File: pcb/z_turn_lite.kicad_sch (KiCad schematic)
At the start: 1 part

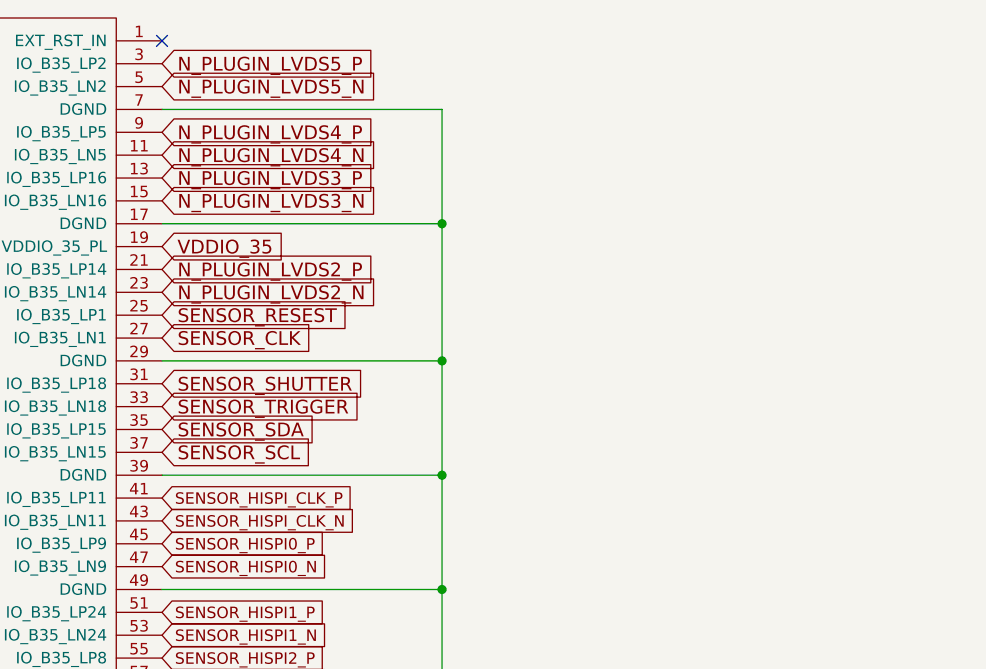
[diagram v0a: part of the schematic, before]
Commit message: refinements; add ar1335 footprint
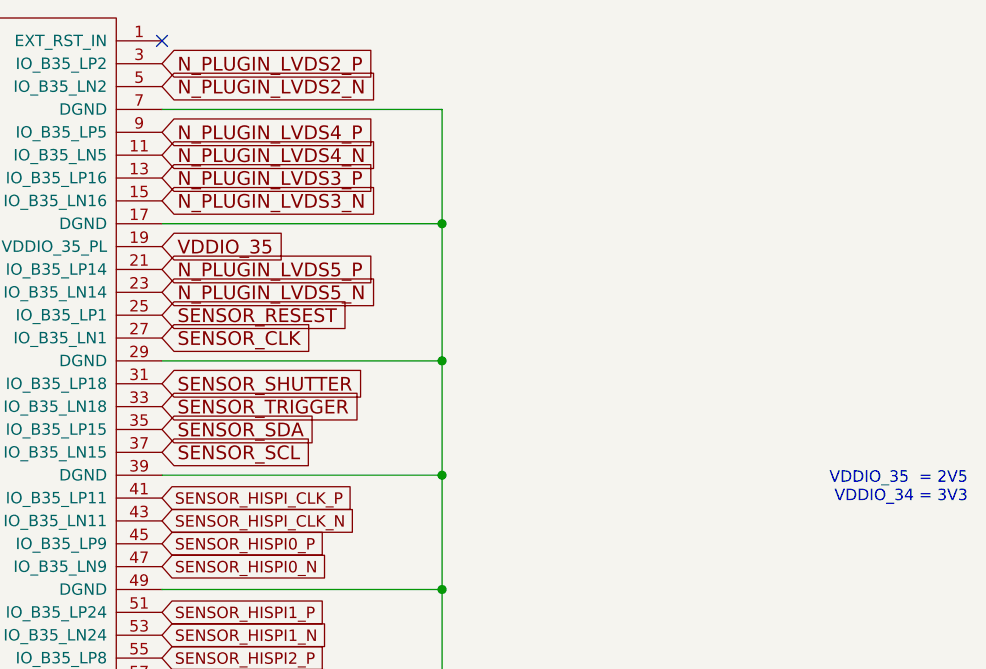
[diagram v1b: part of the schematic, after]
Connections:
- net N_PLUGIN_LVDS2_N: now also A.5 (IO_B35_LN2); no longer A.23 (IO_B35_LN14)
- net N_PLUGIN_LVDS2_P: now also A.3 (IO_B35_LP2); no longer A.21 (IO_B35_LP14)
- net N_PLUGIN_LVDS5_N: now also A.23 (IO_B35_LN14); no longer A.5 (IO_B35_LN2)
- net N_PLUGIN_LVDS5_P: now also A.21 (IO_B35_LP14); no longer A.3 (IO_B35_LP2)
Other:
- note added: "VDDIO_35 = 2V5 VDDIO_34 = 3V3"
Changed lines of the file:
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@@
     (stroke (width 0) (type solid) (color 0 0 0 0))
+  )
+  (text "VDDIO_35  = 2V5\nVDDIO_34 = 3V3" (at 210.82 76.2 180)
+    (effects (font (size 1.27 1.27)) (justify right bottom))
   )
   (global_label "N_PLUGIN_LVDS1_P" (shape input) (at 71.755 27.305 180)    (property "Intersheet References" "${INTERSHEET_REFS}" (id 0) (at 45.4043 27.4002 0)
@@
     (effects (font (size 1.524 1.524)) (justify right))
   )
-  (global_label "N_PLUGIN_LVDS5_P" (shape input) (at 121.285 27.305 0)    (property "Intersheet References" "${INTERSHEET_REFS}" (id 0) (at 147.6357 27.4002 0)
-      (effects (font (size 1.524 1.524)) (justify left) hide)
-    )
-    (effects (font (size 1.524 1.524)) (justify left))
-  )
-  (global_label "N_PLUGIN_LVDS5_N" (shape input) (at 121.285 29.845 0)    (property "Intersheet References" "${INTERSHEET_REFS}" (id 0) (at 147.7083 29.9402 0)
+  (global_label "N_PLUGIN_LVDS2_P" (shape input) (at 121.285 27.305 0)    (property "Intersheet References" "${INTERSHEET_REFS}" (id 0) (at 147.6357 27.2098 0)
+      (effects (font (size 1.524 1.524)) (justify left) hide)
+    )
+    (effects (font (size 1.524 1.524)) (justify left))
+  )
+  (global_label "N_PLUGIN_LVDS2_N" (shape input) (at 121.285 29.845 0)    (property "Intersheet References" "${INTERSHEET_REFS}" (id 0) (at 147.7083 29.7498 0)
       (effects (font (size 1.524 1.524)) (justify left) hide)
     )
@@
     (effects (font (size 1.524 1.524)) (justify left))
   )
-  (global_label "N_PLUGIN_LVDS2_P" (shape input) (at 121.285 50.165 0)    (property "Intersheet References" "${INTERSHEET_REFS}" (id 0) (at 147.6357 50.0698 0)
-      (effects (font (size 1.524 1.524)) (justify left) hide)
-    )
-    (effects (font (size 1.524 1.524)) (justify left))
-  )
-  (global_label "N_PLUGIN_LVDS2_N" (shape input) (at 121.285 52.705 0)    (property "Intersheet References" "${INTERSHEET_REFS}" (id 0) (at 147.7083 52.6098 0)
-      (effects (font (size 1.524 1.524)) (justify left) hide)
-    )
+  (global_label "N_PLUGIN_LVDS5_P" (shape input) (at 121.285 50.165 0)    (property "Intersheet References" "${INTERSHEET_REFS}" (id 0) (at 147.6357 50.2602 0)
+      (effects (font (size 1.524 1.524)) (justify left) hide)
+    )
+    (effects (font (size 1.524 1.524)) (justify left))
+  )
+  (global_label "N_PLUGIN_LVDS5_N" (shape input) (at 121.285 52.705 0)    (property "Intersheet References" "${INTERSHEET_REFS}" (id 0) (at 147.7083 52.8002 0)
+      (effects (font (size 1.524 1.524)) (justify left) hide)
+    )

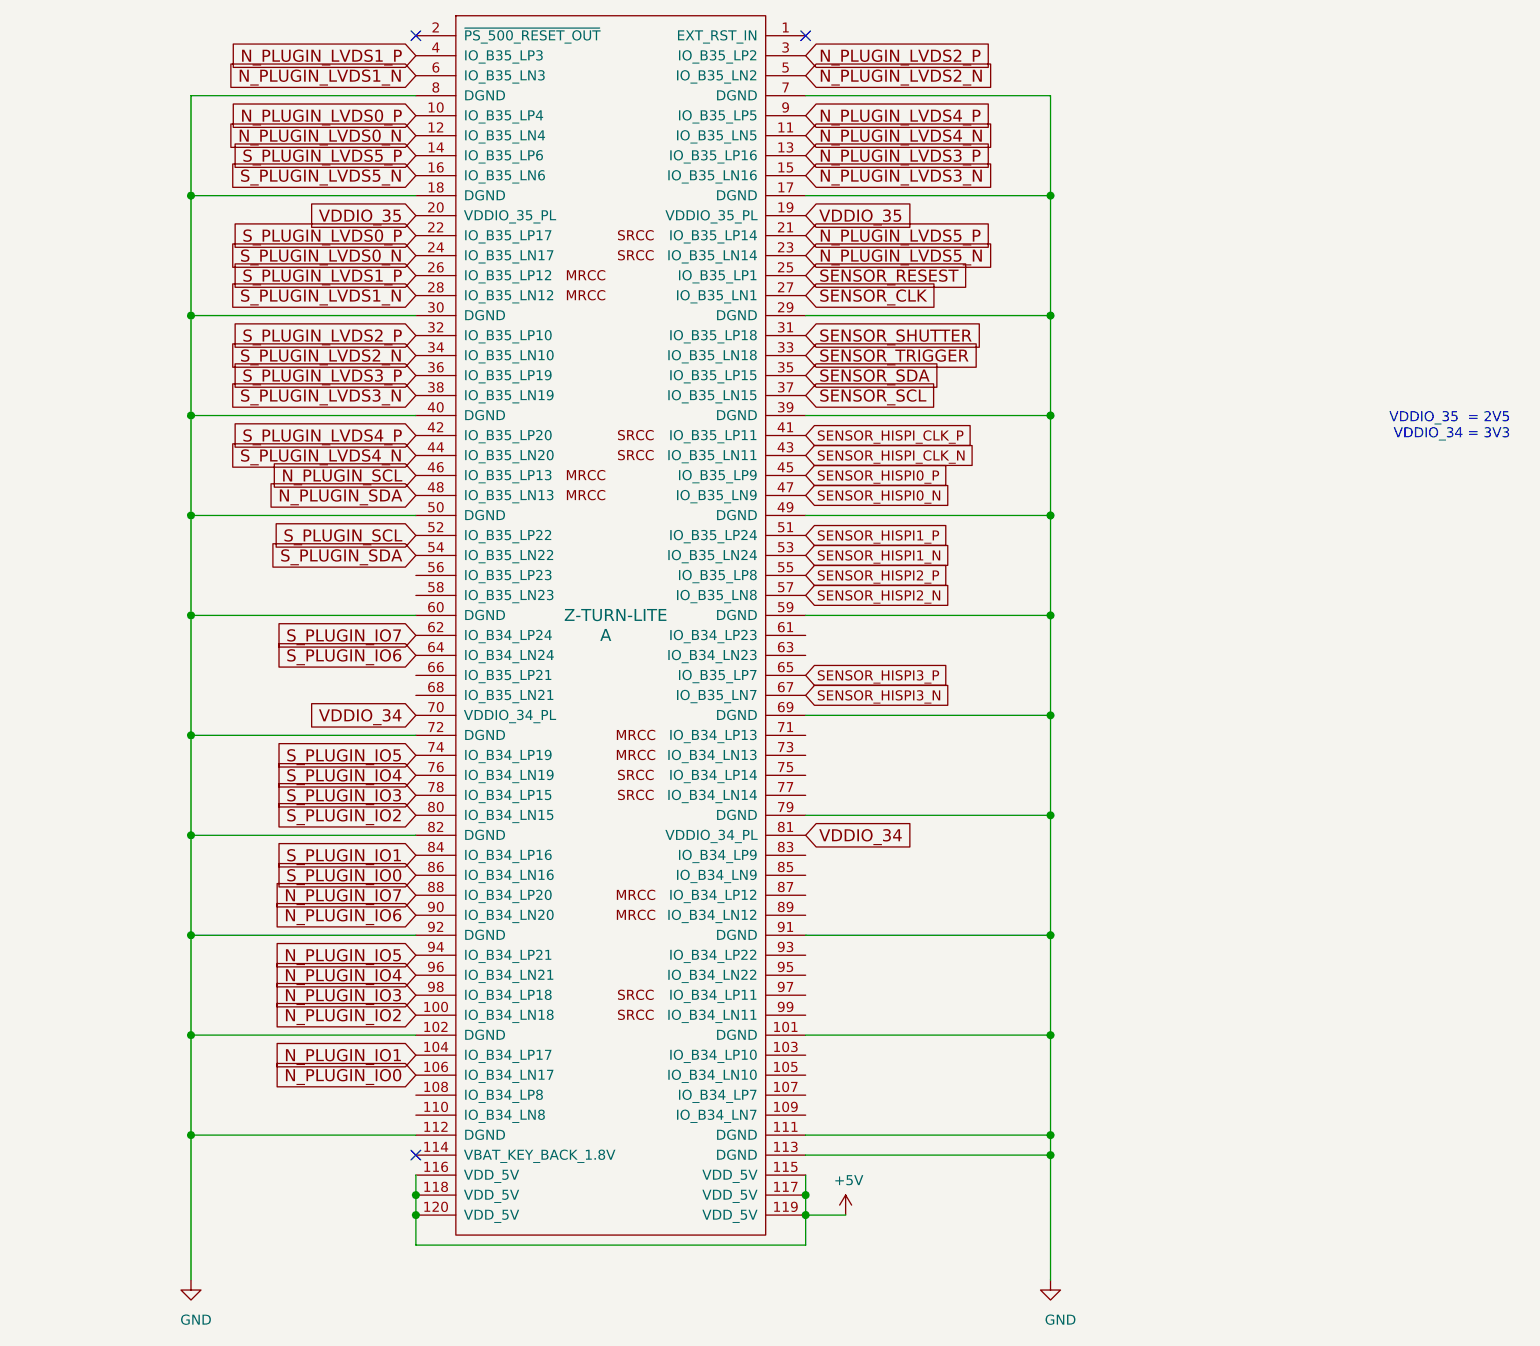
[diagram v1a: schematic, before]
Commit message: Change Plans: two image sensors
* Redo power management
* Add level shifters
* Intention to use both image sensors on the same board
* Add Pmod & LEDs
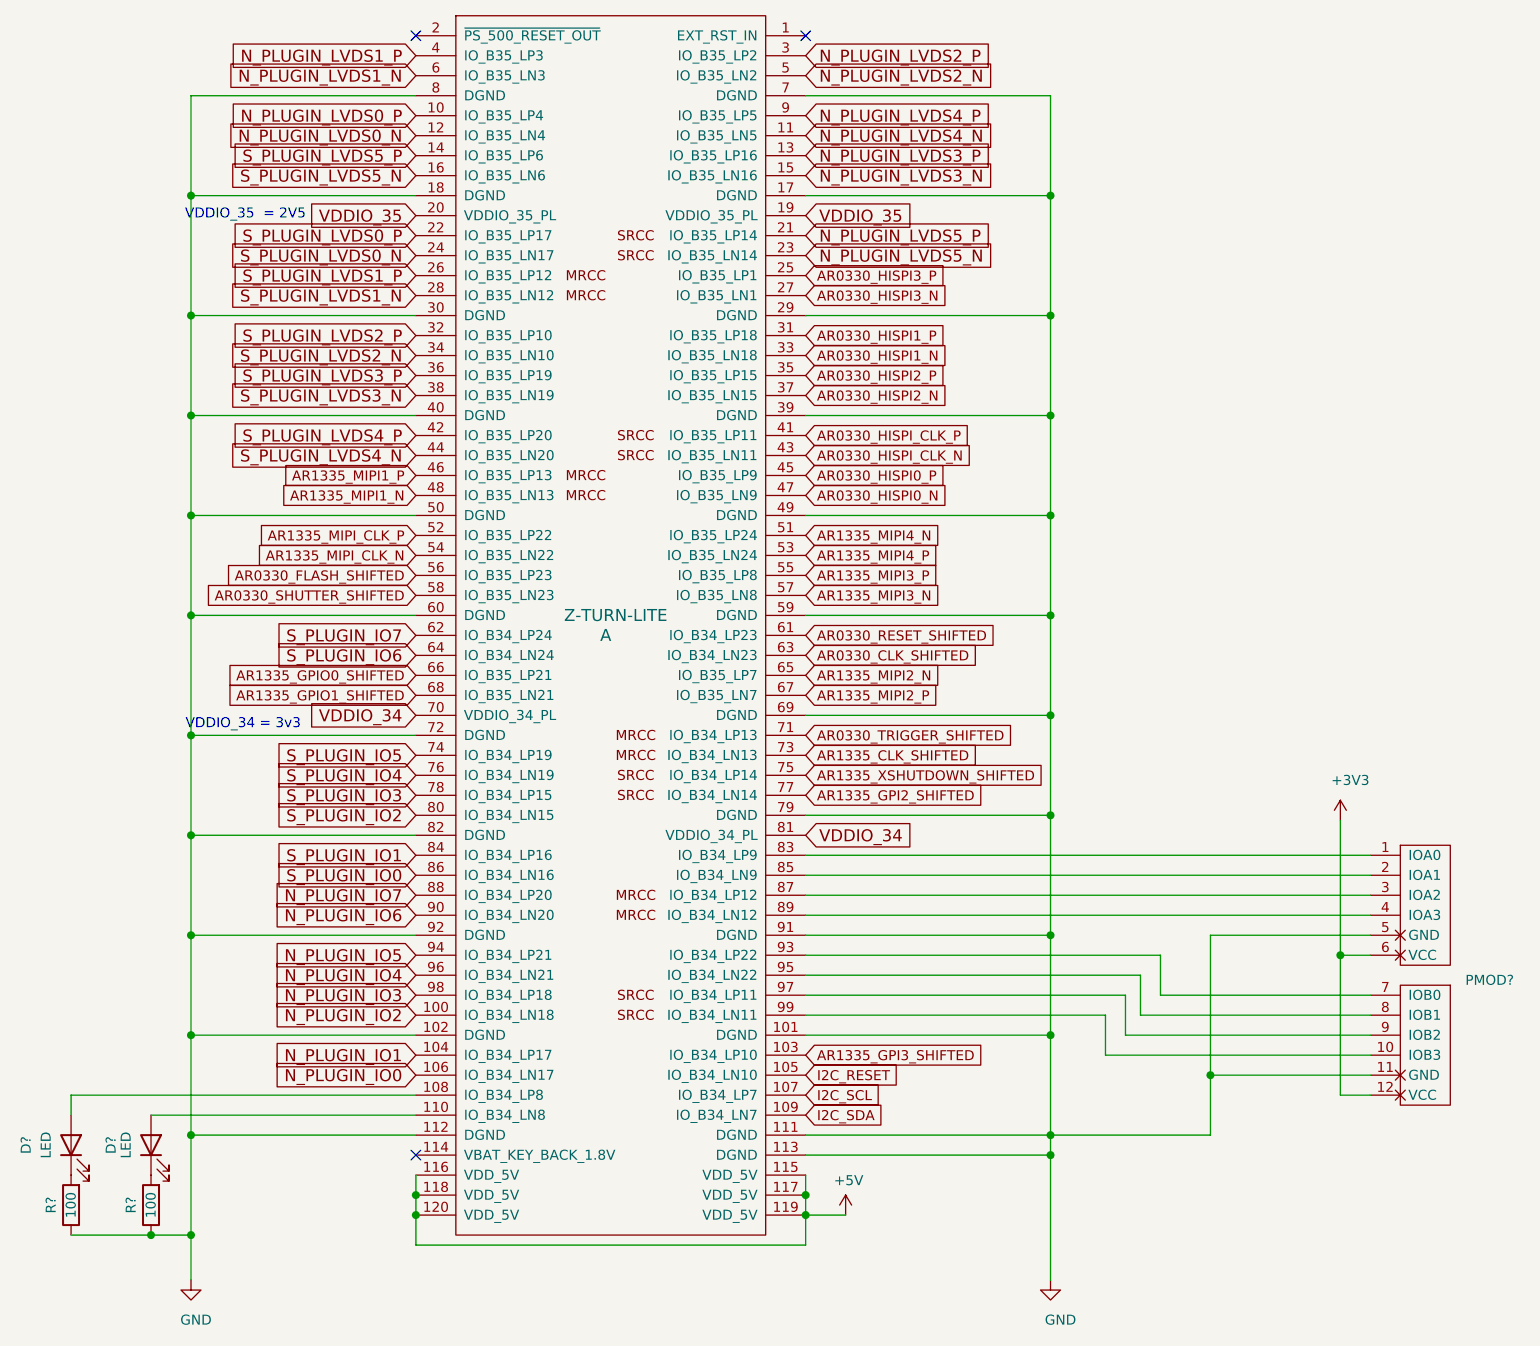
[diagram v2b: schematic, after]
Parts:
- added D? (x2): LED, symbol Device:LED
- added PMOD?: PMOD-Host-x2-GPIO, symbol pmod:PMOD-Host-x2-GPIO
- added R? (x2): 100, symbol Device:R
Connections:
- net GND: now also PMOD?.11 (GND), PMOD?.5 (GND), R?.1, R?.1
- net AR1335_GPI3_SHIFTED: now reaches A.103 (IO_B34_LP10)
- net I2C_RESET: now reaches A.105 (IO_B34_LN10)
- net I2C_SCL: now reaches A.107 (IO_B34_LP7)
- net at A.108 (IO_B34_LP8): now also D?.2 (A)
- net I2C_SDA: now reaches A.109 (IO_B34_LN7)
- net at A.110 (IO_B34_LN8): now also D?.2 (A)
- net AR0330_FLASH_SHIFTED: now reaches A.56 (IO_B35_LP23)
- net AR0330_SHUTTER_SHIFTED: now reaches A.58 (IO_B35_LN23)
- net AR0330_RESET_SHIFTED: now reaches A.61 (IO_B34_LP23)
- net AR0330_CLK_SHIFTED: now reaches A.63 (IO_B34_LN23)
- net AR1335_GPIO0_SHIFTED: now reaches A.66 (IO_B35_LP21)
- net AR1335_GPIO1_SHIFTED: now reaches A.68 (IO_B35_LN21)
- net AR0330_TRIGGER_SHIFTED: now reaches A.71 (IO_B34_LP13)
- net AR1335_CLK_SHIFTED: now reaches A.73 (IO_B34_LN13)
- net AR1335_XSHUTDOWN_SHIFTED: now reaches A.75 (IO_B34_LP14)
- net AR1335_GPI2_SHIFTED: now reaches A.77 (IO_B34_LN14)
- net at A.83 (IO_B34_LP9): now also PMOD?.1 (IOA0)
- net at A.85 (IO_B34_LN9): now also PMOD?.2 (IOA1)
- net at A.87 (IO_B34_LP12): now also PMOD?.3 (IOA2)
- net at A.89 (IO_B34_LN12): now also PMOD?.4 (IOA3)
- net at A.93 (IO_B34_LP22): now also PMOD?.7 (IOB0)
- net at A.95 (IO_B34_LN22): now also PMOD?.8 (IOB1)
- net at A.97 (IO_B34_LP11): now also PMOD?.9 (IOB2)
- net at A.99 (IO_B34_LN11): now also PMOD?.10 (IOB3)
- net N_PLUGIN_SCL renamed AR1335_MIPI1_P
- net N_PLUGIN_SDA renamed AR1335_MIPI1_N
- net SENSOR_CLK renamed AR0330_HISPI3_N
- net SENSOR_HISPI0_N renamed AR0330_HISPI0_N
- net SENSOR_HISPI0_P renamed AR0330_HISPI0_P
- net SENSOR_HISPI1_N renamed AR1335_MIPI4_P
- net SENSOR_HISPI1_P renamed AR1335_MIPI4_N
- net SENSOR_HISPI2_N renamed AR1335_MIPI3_N
- net SENSOR_HISPI2_P renamed AR1335_MIPI3_P
- net SENSOR_HISPI3_N renamed AR1335_MIPI2_P
- net SENSOR_HISPI3_P renamed AR1335_MIPI2_N
- net SENSOR_HISPI_CLK_N renamed AR0330_HISPI_CLK_N
- net SENSOR_HISPI_CLK_P renamed AR0330_HISPI_CLK_P
- net SENSOR_RESEST renamed AR0330_HISPI3_P
- net SENSOR_SCL renamed AR0330_HISPI2_N
- net SENSOR_SDA renamed AR0330_HISPI2_P
- net SENSOR_SHUTTER renamed AR0330_HISPI1_P
- net SENSOR_TRIGGER renamed AR0330_HISPI1_N
- net S_PLUGIN_SCL renamed AR1335_MIPI_CLK_P
- net S_PLUGIN_SDA renamed AR1335_MIPI_CLK_N
- new net: D?.1 (K), R?.2 (x2)
- new net +3V3: PMOD?.12 (VCC), PMOD?.6 (VCC)
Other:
- note added: "VDDIO_34 = 3v3"
- note added: "VDDIO_35 = 2V5"
- note removed: "VDDIO_35 = 2V5 VDDIO_34 = 3V3"

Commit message: add i2c addresses
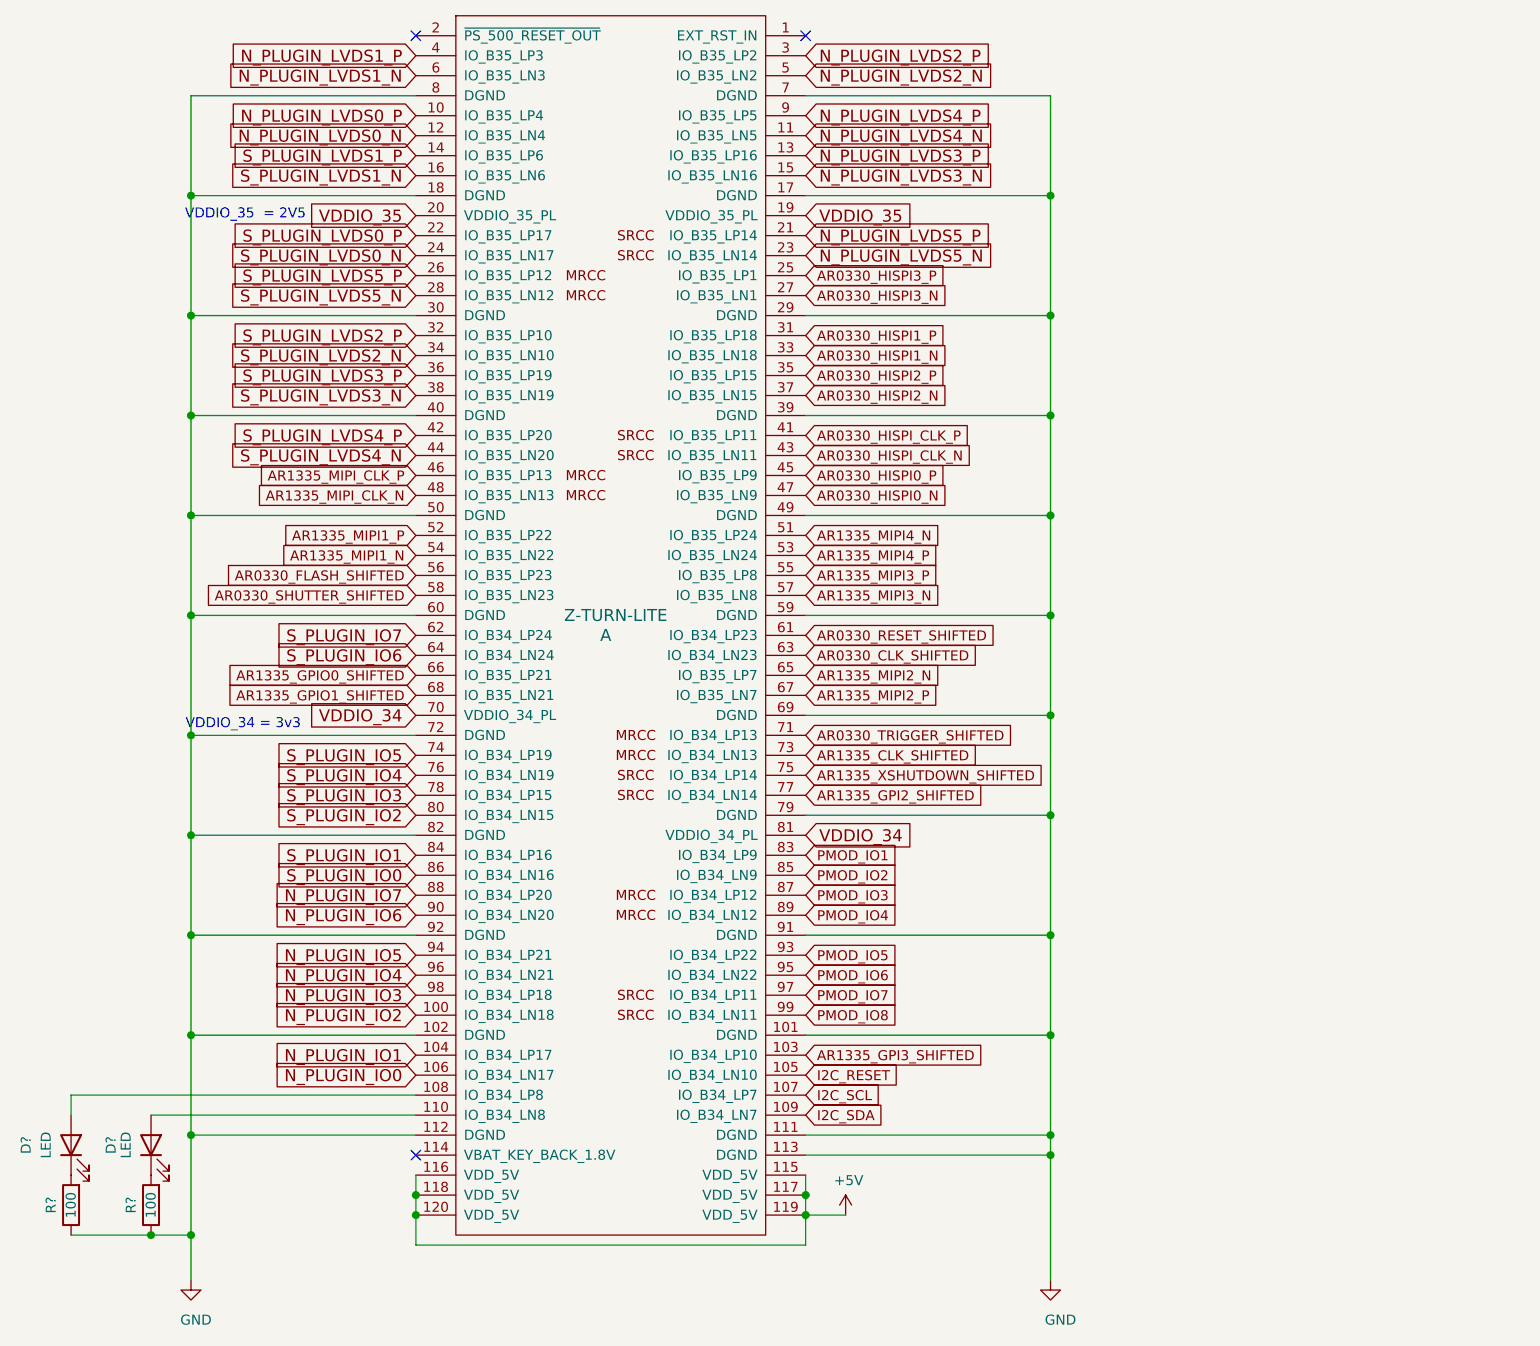
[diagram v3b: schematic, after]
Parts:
- removed PMOD?: PMOD-Host-x2-GPIO, symbol pmod:PMOD-Host-x2-GPIO
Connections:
- net AR1335_MIPI1_N: now also A.54 (IO_B35_LN22); no longer A.48 (IO_B35_LN13)
- net AR1335_MIPI1_P: now also A.52 (IO_B35_LP22); no longer A.46 (IO_B35_LP13)
- net AR1335_MIPI_CLK_N: now also A.48 (IO_B35_LN13); no longer A.54 (IO_B35_LN22)
- net AR1335_MIPI_CLK_P: now also A.46 (IO_B35_LP13); no longer A.52 (IO_B35_LP22)
- net S_PLUGIN_LVDS1_N: now also A.16 (IO_B35_LN6); no longer A.28 (IO_B35_LN12)
- net S_PLUGIN_LVDS1_P: now also A.14 (IO_B35_LP6); no longer A.26 (IO_B35_LP12)
- net S_PLUGIN_LVDS5_N: now also A.28 (IO_B35_LN12); no longer A.16 (IO_B35_LN6)
- net S_PLUGIN_LVDS5_P: now also A.26 (IO_B35_LP12); no longer A.14 (IO_B35_LP6)
- net PMOD_IO1: now reaches A.83 (IO_B34_LP9)
- net PMOD_IO2: now reaches A.85 (IO_B34_LN9)
- net PMOD_IO3: now reaches A.87 (IO_B34_LP12)
- net PMOD_IO4: now reaches A.89 (IO_B34_LN12)
- net PMOD_IO5: now reaches A.93 (IO_B34_LP22)
- net PMOD_IO6: now reaches A.95 (IO_B34_LN22)
- net PMOD_IO7: now reaches A.97 (IO_B34_LP11)
- net PMOD_IO8: now reaches A.99 (IO_B34_LN11)
